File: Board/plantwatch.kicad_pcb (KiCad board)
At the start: 2 copper layers, 159.9 x 99.9 mm, 41 parts, among them IC1 HS1101, J1 Motor Connector, J2 Sensor Connector, J5 nRF24L01P Connector, Q1 BSP129, SW1 SW_Push, SW2 SW_Push, U1 MKL25Z128VLK4, U2 TMP36, U4 NCP1117-3.3_SOT223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

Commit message: Make layout
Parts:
- C1, C7: value C_Small -> 0.2uF
- moved C14 157.4 mm to (150.4, 114.9)
- moved C4 157.4 mm to (146.0, 133.6)
- moved C2 157.4 mm to (137.5, 130.0)
- moved C5 157.4 mm to (155.8, 125.1)
- moved R4 135.4 mm to (97.0, 80.2)
- moved C15 124.9 mm to (130.0, 56.0)
- moved C10 123.3 mm to (105.9, 87.8), turned to 270 degrees
- moved R5 115.5 mm to (97.0, 84.6)
- moved R2 109.6 mm to (85.6, 106.8), turned to 90 degrees
- moved C3 109.5 mm to (114.8, 56.0)
- moved C9 108.0 mm to (97.0, 75.1)
- moved C6 108.0 mm to (95.7, 89.7)
- moved R3 98.4 mm to (80.5, 94.1), turned to 270 degrees
- moved R8 85.2 mm to (89.4, 95.4)
- moved C7 84.5 mm to (77.9, 84.6), turned to 180 degrees
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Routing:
- net NRF24L01P_IRQ: track 0.00 -> 28.8 mm, vias 0 -> 2
- net Net-(C12-Pad2): track 0.00 -> 26.1 mm
- net NRF24L01P_CE: track 0.00 -> 20.4 mm, vias 0 -> 2
- net Net-(C13-Pad1): track 0.00 -> 20.2 mm
- net +3V3: track 0.00 -> 18.9 mm, vias 0 -> 2
- net Net-(IC1-Pad2): track 0.00 -> 15.5 mm
- net TMP36GT: track 0.00 -> 15.3 mm
- net SEN0193: track 0.00 -> 14.1 mm
- net Net-(C8-Pad1): track 0.00 -> 12.3 mm
- net NRF24L01P_MOSI: track 0.00 -> 9.84 mm
- net NRF24L01P_MISO: track 0.00 -> 9.11 mm
- net NRF24L01P_CSN: track 0.00 -> 9.08 mm
- net NRF24L01P_SCK: track 0.00 -> 7.15 mm
- net HS1101: track 0.00 -> 5.41 mm
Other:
- board size 159.9 x 99.9 mm -> 159.9 x 101.1 mm

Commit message: PCB almost done
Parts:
- removed C16: C_Small, Capacitor_THT:CP_Radial_Tantal_D4.5mm_P5.00mm
- removed C7: 0.2uF, Capacitor_THT:CP_Radial_Tantal_D4.5mm_P5.00mm
- removed J5: nRF24L01P Connector, Connector_PinSocket_2.54mm:PinSocket_2x04_P2.54mm_Vertical
- removed R9: 10K, Resistor_THT:R_Axial_DIN0411_L9.9mm_D3.6mm_P12.70mm_Horizontal
- removed SW2: SW_Push, Button_Switch_THT:SW_PUSH_6mm
- added J3: SWD, Connector_PinHeader_1.00mm:PinHeader_2x05_P1.00mm_Vertical_SMD, F.Cu at (71.0, 118.3)
- added J6: Power Input, Connector_BarrelJack:BarrelJack_Horizontal, F.Cu at (147.2, 92.2)
- added U3: nRF24L01+, RF_Module:nRF24L01_Breakout, F.Cu at (91.9, 89.7)
- C1: value 0.2uF -> 0.1uF; footprint Capacitor_THT:CP_Radial_Tantal_D4.5mm_P5.00mm -> Capacitor_Tantalum_SMD:CP_EIA-3528-15_AVX-H_Pad1.50x2.35mm_HandSolder
- C10, C11, C12, C13, C8, C9: footprint Capacitor_THT:CP_Radial_Tantal_D4.5mm_P5.00mm -> Capacitor_Tantalum_SMD:CP_EIA-3528-15_AVX-H_Pad1.50x2.35mm_HandSolder
- C14: value 1uF -> 0.1uF; footprint Capacitor_THT:CP_Radial_Tantal_D4.5mm_P5.00mm -> Capacitor_Tantalum_SMD:CP_EIA-3528-15_AVX-H_Pad1.50x2.35mm_HandSolder
- C15, C2, C3, C6: value C_Small -> 0.1uF; footprint Capacitor_THT:CP_Radial_Tantal_D4.5mm_P5.00mm -> Capacitor_Tantalum_SMD:CP_EIA-3528-15_AVX-H_Pad1.50x2.35mm_HandSolder
- C4, C5: value C_Small -> 0.1uF; footprint Capacitor_THT:CP_Radial_Tantal_D4.5mm_P5.00mm -> Capacitor_Tantalum_SMD:CP_EIA-3528-15_AVX-H_Pad1.50x2.35mm_HandSolder; moved to B.Cu
- J1: value Motor Connector -> Motor
- J2: value Sensor Connector -> SEN0193
- R1, R2, R3, R4, R5, R6, R7, R8: footprint Resistor_THT:R_Axial_DIN0411_L9.9mm_D3.6mm_P12.70mm_Horizontal -> Resistor_SMD:R_2512_6332Metric_Pad1.52x3.35mm_HandSolder
- SW1: value SW_Push -> Reset
- U4: value NCP1117-3.3_SOT223 -> +12V Regulator
- Y1: value Crystal_GND24 -> 8 MHz
- moved R1 137.6 mm to (68.4, 126.3), turned to 90 degrees
- moved SW1 134.6 mm to (76.7, 125.9)
- moved C8 129.3 mm to (72.9, 126.5), turned to 270 degrees
- moved R6 95.9 mm to (113.5, 92.2), turned to 0 degrees
- moved J1 88.1 mm to (125.6, 84.6), turned to 90 degrees
- moved D1 87.2 mm to (130.0, 84.6), turned to 270 degrees
- moved R7 85.0 mm to (113.5, 87.8), turned to 180 degrees
- moved Q1 78.8 mm to (117.3, 80.8), turned to 180 degrees
- moved U4 69.5 mm to (138.9, 97.9), turned to 180 degrees
- moved C2 68.4 mm to (71.2, 113.2)
- moved C11 66.1 mm to (138.3, 86.2)
- moved C1 64.5 mm to (141.7, 92.2), turned to 180 degrees
- moved C4 58.6 mm to (90.6, 114.5), turned to 180 degrees
- moved IC1 56.5 mm to (126.8, 110.0)
- moved C15 53.3 mm to (141.2, 108.1)
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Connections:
- C1 pad 1: +3V3 -> +12V
- C14 pad 1: Net-(C14-Pad1) -> +12V
- C14 pad 2: GND -> Net-(C14-Pad2)
- D1 pad 2: GND -> Net-(C14-Pad2)
- J1 pad 2: GND -> Net-(C14-Pad2)
- Q1 pad 1: GND -> Net-(C14-Pad2)
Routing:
- net +3V3: track 18.9 -> 171.1 mm, vias 2 -> 4
- net Net-(R5-Pad2): track 0.00 -> 54.1 mm
- net Net-(J3-Pad4): track 0.00 -> 41.5 mm
- net Net-(J2-Pad1): track 0.00 -> 40.5 mm
- net +12V: track 0.00 -> 35.9 mm
- net Net-(C8-Pad1): track 12.3 -> 42.8 mm
- net Net-(J3-Pad2): track 0.00 -> 29.7 mm
- net Net-(C14-Pad2): track 0.00 -> 25.6 mm
- net Net-(Q1-Pad2): track 0.00 -> 21.4 mm
- net HS1101: track 5.41 -> 22.1 mm
- net NRF24L01P_SCK: track 7.15 -> 22.8 mm
- net MOTOR: track 0.00 -> 15.5 mm
- net NRF24L01P_MISO: track 9.11 -> 24.4 mm
- net NRF24L01P_MOSI: track 9.84 -> 24.7 mm
- net NRF24L01P_CSN: track 9.08 -> 23.1 mm
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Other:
- board size 159.9 x 101.1 mm -> 113 x 83.8 mm
- board text added: "+12V"
- board text added: "8MHz crystal"
- board text added: "Reset MCU"
- board text added: "SWD"
- board text added: "Sensors"
- board text added: "nRF24L01+"

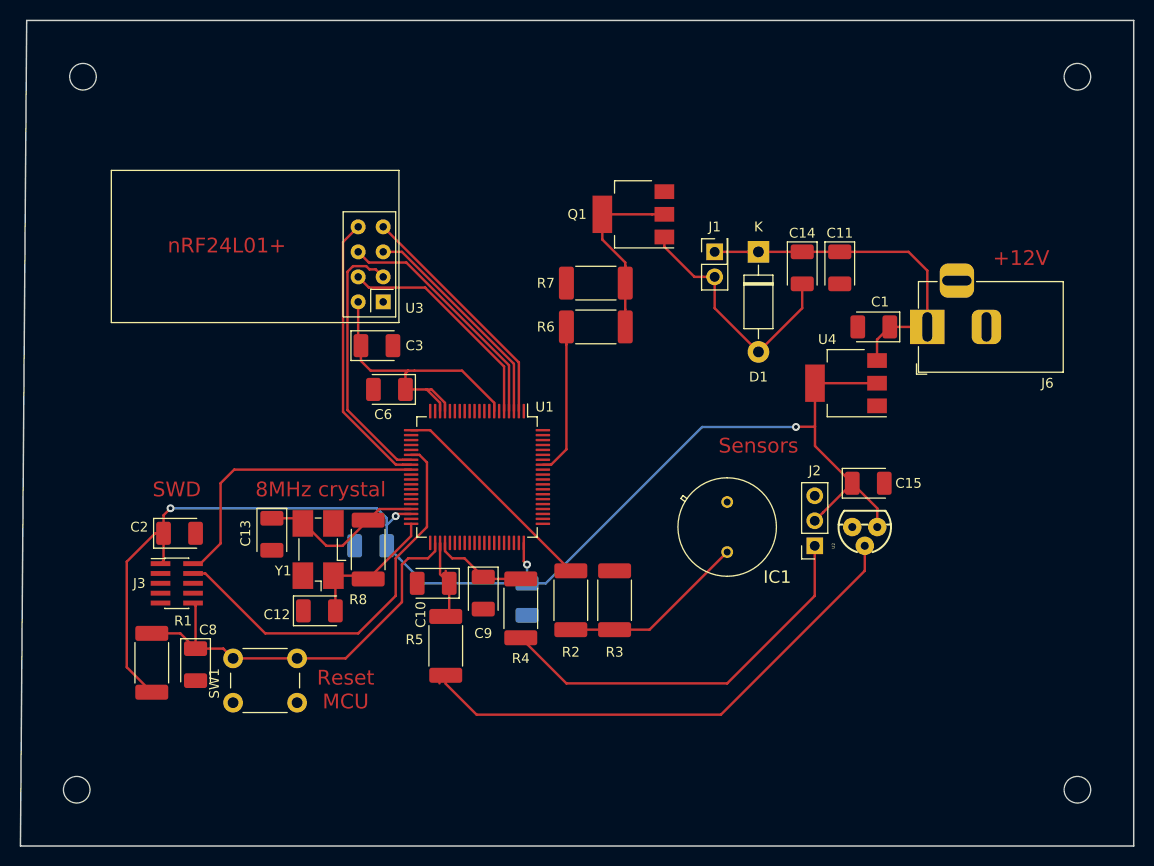
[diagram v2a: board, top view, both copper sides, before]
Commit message: Adding copper pous
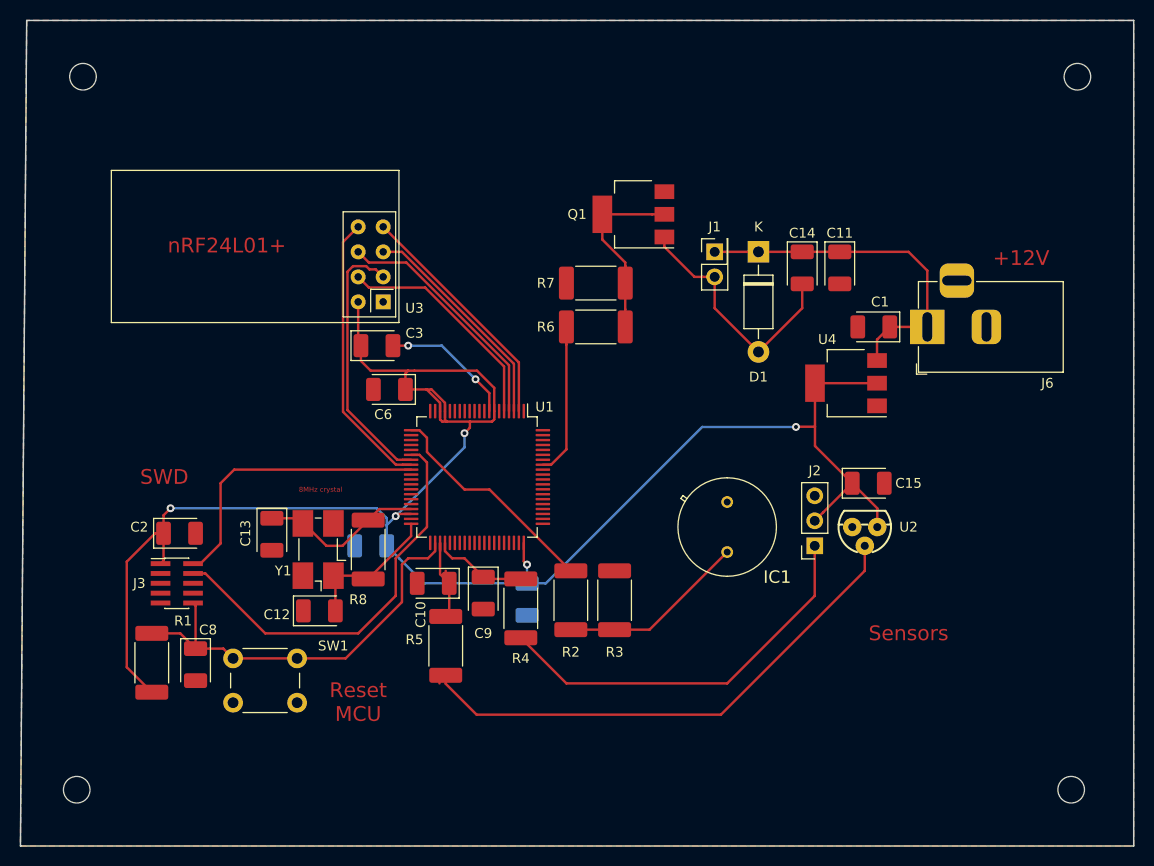
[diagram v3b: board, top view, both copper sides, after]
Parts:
- moved MK4 0.64 mm to (161.8, 139.2)
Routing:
- net +3V3: track 171.1 -> 193.2 mm, vias 4 -> 5
- net GND: track 0.00 -> 13.6 mm, vias 0 -> 2
- net HS1101: track 22.1 -> 23.0 mm
- added copper zone on B.Cu, net GND
- added copper zone on F.Cu, net GND
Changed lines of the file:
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@@
     (thickness 1.6)
     (drawings 10)
-    (tracks 185)
+    (tracks 210)
     (zones 0)
     (modules 39)
@@
     (tags "capacitor tantalum")
     (attr smd)
-    (fp_text reference C3 (at 3.81 0 180) (layer F.SilkS)
+    (fp_text reference C3 (at 3.81 -1.27 180) (layer F.SilkS)
       (effects (font (size 1 1) (thickness 0.15)))
     )
@@
   )
   (module Mounting_Holes:MountingHole_2.7mm (layer F.Cu)
-    (at 162.395 139.215)
+    (at 161.76 139.215)
     (descr "Mounting Hole 2.7mm, no annular")
     (tags "mounting hole 2.7mm no annular")
@@
       (effects (font (size 1 1) (thickness 0.15)))
     )
+    (fp_circle (center 0 0) (end 2.7 0) (layer Cmts.User) (width 0.15))
     (fp_circle (center 0 0) (end 2.95 0) (layer F.CrtYd) (width 0.05))
-    (fp_circle (center 0 0) (end 2.7 0) (layer Cmts.User) (width 0.15))
     (pad 1 np_thru_hole circle (at 0 0) (size 2.7 2.7) (drill 2.7) (layers *.Cu *.Mask)
       (net 4 "Net-(MK4-Pad1)"))
@@
     (descr https://www.omron.com/ecb/products/pdf/en-b3f.pdf)
     (tags "tact sw push 6mm")
-    (fp_text reference SW1 (at -1.905 2.54 90) (layer F.SilkS)
+    (fp_text reference SW1 (at 10.16 -1.27 180) (layer F.SilkS)
       (effects (font (size 1 1) (thickness 0.15)))
     )
@@
     (at 140.805 112.545 180)
     (descr "<b>TO 92</b>")
-    (fp_text reference U2 (at 3.175 -1.905 90) (layer F.SilkS)
-      (effects (font (size 0.320045 0.320045) (thickness 0.015)))
-    )
-    (fp_text value TMP36 (at -1.905 -3.81 90) (layer F.Fab)
-      (effects (font (size 0.320413 0.320413) (thickness 0.015)))
+    (fp_text reference U2 (at -4.445 0 180) (layer F.SilkS)
+      (effects (font (size 1 1) (thickness 0.15)))
+    )
+    (fp_text value TMP36 (at -5.715 -1.27 180) (layer F.Fab)
+      (effects (font (size 1 1) (thickness 0.15)))
     )
     (fp_arc (start -0.000001 0.000003) (end -0.7863 -2.5485) (angle -111.099) (layer F.SilkS) (width 0.2032))
@@
   (gr_line (start 55.08 144.93) (end 168.11 144.93) (layer Edge.Cuts) (width 0.15))
   (gr_line (start 55.715 61.11) (end 55.08 144.93) (layer Edge.Cuts) (width 0.15))
-  (gr_text Sensors (at 130.01 104.29) (layer F.Cu)
+  (gr_text Sensors (at 145.25 123.34) (layer F.Cu)
     (effects (font (size 1.5 1.5) (thickness 0.3)))
   )
-  (gr_text "Reset\nMCU" (at 88.1 129.055) (layer F.Cu)
+  (gr_text "Reset\nMCU" (at 89.37 130.325) (layer F.Cu)
     (effects (font (size 1.5 1.5) (thickness 0.3)))
   )
-  (gr_text SWD (at 70.955 108.735) (layer F.Cu)
+  (gr_text SWD (at 69.685 107.465) (layer F.Cu)
     (effects (font (size 1.5 1.5) (thickness 0.3)))
   )
@@
   )
   (gr_text "8MHz crystal" (at 85.56 108.735) (layer F.Cu)
-    (effects (font (size 1.5 1.5) (thickness 0.3)))
+    (effects (font (size 0.5 0.5) (thickness 0.1)))
   )
   (gr_text nRF24L01+ (at 76.035 83.97) (layer F.Cu)
     (effects (font (size 1.5 1.5) (thickness 0.3)))
   )
+  (via (at 101.284847 97.545153) (size 0.8) (drill 0.4) (layers F.Cu B.Cu) (net 5))
+  (segment (start 102.685 100.7775) (end 102.685 98.945306) (width 0.25) (layer F.Cu) (net 5))
+  (segment (start 102.685 98.945306) (end 101.284847 97.545153) (width 0.25) (layer F.Cu) (net 5))
+  (via (at 94.45 94.13) (size 0.8) (drill 0.4) (layers F.Cu B.Cu) (net 5))
+  (segment (start 101.284847 97.545153) (end 97.869694 94.13) (width 0.25) (layer B.Cu) (net 5))
+  (segment (start 97.869694 94.13) (end 94.45 94.13) (width 0.25) (layer B.Cu) (net 5))
+  (segment (start 94.45 94.13) (end 92.9 94.13) (width 0.25) (layer F.Cu) (net 5))
   (segment (start 89.37 93.85) (end 89.65 94.13) (width 0.25) (layer F.Cu) (net 6))
   (segment (start 89.37 89.685) (end 89.37 93.85) (width 0.25) (layer F.Cu) (net 6))
   (segment (start 89.65 94.13) (end 89.65 95.68) (width 0.25) (layer F.Cu) (net 6))
   (segment (start 89.65 95.68) (end 90.64 96.67) (width 0.25) (layer F.Cu) (net 6))
-  (segment (start 103.185 99.94) (end 103.185 100.7775) (width 0.25) (layer F.Cu) (net 6))
-  (segment (start 99.915 96.67) (end 103.185 99.94) (width 0.25) (layer F.Cu) (net 6))
-  (segment (start 95.085 96.67) (end 99.915 96.67) (width 0.25) (layer F.Cu) (net 6))
   (segment (start 97.685 99.94) (end 97.685 100.7775) (width 0.25) (layer F.Cu) (net 6))
   (segment (start 96.32 98.575) (end 97.685 99.94) (width 0.25) (layer F.Cu) (net 6))
@@
   (segment (start 94.17 98.575) (end 94.17 96.95) (width 0.25) (layer F.Cu) (net 6))
   (segment (start 90.64 96.67) (end 94.45 96.67) (width 0.25) (layer F.Cu) (net 6))
-  (segment (start 94.45 96.67) (end 95.085 96.67) (width 0.25) (layer F.Cu) (net 6))
   (segment (start 142.05 97.94) (end 135.75 97.94) (width 0.25) (layer F.Cu) (net 6))
   (segment (start 136.574999 111.060001) (end 139.535 108.1) (width 0.25) (layer F.Cu) (net 6))
@@
   (segment (start 93.535 115.72) (end 92.265 114.45) (width 0.25) (layer B.Cu) (net 6))
   (segment (start 92.265 114.45) (end 92.265 112.355) (width 0.25) (layer B.Cu) (net 6))
+  (segment (start 103.185 101.615) (end 103.185 100.7775) (width 0.25) (layer F.Cu) (net 6))
+  (segment (start 102.95999 101.84001) (end 103.185 101.615) (width 0.25) (layer F.Cu) (net 6))
+  (segment (start 97.685 101.615) (end 97.91001 101.84001) (width 0.25) (layer F.Cu) (net 6))
+  (segment (start 97.685 100.7775) (end 97.685 101.615) (width 0.25) (layer F.Cu) (net 6))
+  (segment (start 98.185 101.675) (end 98.35001 101.84001) (width 0.25) (layer F.Cu) (net 6))
+  (segment (start 98.185 100.7775) (end 98.185 101.675) (width 0.25) (layer F.Cu) (net 6))
+  (segment (start 97.91001 101.84001) (end 98.35001 101.84001) (width 0.25) (layer F.Cu) (net 6))
+  (segment (start 95.085 96.67) (end 94.45 96.67) (width 0.25) (layer F.Cu) (net 6))
+  (segment (start 101.435 96.67) (end 95.085 96.67) (width 0.25) (layer F.Cu) (net 6))
+  (segment (start 103.185 100.7775) (end 103.185 98.42) (width 0.25) (layer F.Cu) (net 6))
+  (segment (start 103.185 98.42) (end 101.435 96.67) (width 0.25) (layer F.Cu) (net 6))
+  (via (at 100.165 103.02) (size 0.8) (drill 0.4) (layers F.Cu B.Cu) (net 6))
+  (segment (start 100.70999 102.47501) (end 100.165 103.02) (width 0.25) (layer F.Cu) (net 6))
+  (segment (start 100.70999 101.84001) (end 100.70999 102.47501) (width 0.25) (layer F.Cu) (net 6))
+  (segment (start 100.70999 101.84001) (end 102.95999 101.84001) (width 0.25) (layer F.Cu) (net 6))
+  (segment (start 98.35001 101.84001) (end 100.70999 101.84001) (width 0.25) (layer F.Cu) (net 6))
+  (segment (start 100.165 104.455) (end 93.18 111.44) (width 0.25) (layer B.Cu) (net 6))
+  (segment (start 100.165 103.02) (end 100.165 104.455) (width 0.25) (layer B.Cu) (net 6))
   (segment (start 76.2225 125.4325) (end 76.67 125.88) (width 0.25) (layer F.Cu) (net 7))
   (segment (start 76.67 125.88) (end 83.17 125.88) (width 0.25) (layer F.Cu) (net 7))
@@
   (segment (start 114.16 80.795) (end 114.16 83.36) (width 0.25) (layer F.Cu) (net 21))
   (segment (start 114.16 83.36) (end 116.4875 85.6875) (width 0.25) (layer F.Cu) (net 21))
-  (segment (start 96.685 102.715) (end 94.7475 102.715) (width 0.25) (layer F.Cu) (net 22))
-  (segment (start 110.96 116.99) (end 96.685 102.715) (width 0.25) (layer F.Cu) (net 22))
+  (segment (start 110.96 116.99) (end 102.705 108.735) (width 0.25) (layer F.Cu) (net 22))
+  (segment (start 102.705 108.735) (end 100.165 108.735) (width 0.25) (layer F.Cu) (net 22))
+  (segment (start 100.165 108.735) (end 96.355 104.925) (width 0.25) (layer F.Cu) (net 22))
+  (segment (start 95.585 102.715) (end 94.7475 102.715) (width 0.25) (layer F.Cu) (net 22))
+  (segment (start 96.355 103.485) (end 95.585 102.715) (width 0.25) (layer F.Cu) (net 22))
+  (segment (start 96.355 104.925) (end 96.355 103.485) (width 0.25) (layer F.Cu) (net 22))
   (segment (start 97.625 128.42) (end 97.625 127.5975) (width 0.25) (layer F.Cu) (net 23))
   (segment (start 140.805 116.99) (end 140.805 114.45) (width 0.25) (layer F.Cu) (net 23))
@@
   (segment (start 134.455 90.32) (end 134.455 87.855) (width 0.25) (layer F.Cu) (net 86))
   (segment (start 130.01 94.765) (end 134.455 90.32) (width 0.25) (layer F.Cu) (net 86))
+  (zone (net 5) (net_name GND) (layer F.Cu) (hatch edge 0.508)
+    (connect_pads (clearance 0.508))
+    (min_thickness 0.254)
+    (fill yes (arc_segments 32) (thermal_gap 0.508) (thermal_bridge_width 0.508))
+    (polygon
+      (pts
+        (xy 55.715 61.11) (xy 55.08 144.93) (xy 168.11 144.93) (xy 168.11 61.11)
+      )
+    )
+  )
+  (zone (net 5) (net_name GND) (layer B.Cu) (hatch edge 0.508)
+    (connect_pads (clearance 0.508))
+    (min_thickness 0.254)
+    (fill yes (arc_segments 32) (thermal_gap 0.508) (thermal_bridge_width 0.508))
+    (polygon
+      (pts
+        (xy 55.715 61.11) (xy 55.08 144.93) (xy 168.11 144.93) (xy 168.11 61.11)
+      )
+    )
+  )
 )

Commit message: PCB done
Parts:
- moved SW1 1.27 mm to (76.7, 127.2)
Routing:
- net GND: track 13.6 -> 127.9 mm, vias 2 -> 6
- net +3V3: track 193.2 -> 195.1 mm
- net Net-(J3-Pad4): track 41.5 -> 42.4 mm
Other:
- board text added: "Water Pump"
